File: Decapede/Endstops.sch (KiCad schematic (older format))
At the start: 30 parts, among them P22 X_min, P23 X_max, P24 Y_min, P25 Y_max, P26 Z_min, P27 Z_max, P28 W_min, P29 W_max, P30 V_min, P31 V_max, P32 A_min, P33 A_max, P34 B_min, P35 B_max, P36 C_min, P37 C_max, P38 D_min, P39 D_max, P40 E_min, P41 E_max

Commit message: Updates for Decapede project.
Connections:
- net +5V renamed +V_LOGIC
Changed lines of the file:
@@
 Sheet 5 10
 Title "Endstop connectors"
-Date "19 jan 2014"
+Date "26 jan 2014"
 Rev ""
 Comp ""
@@
 	1    0    0    -1
 $EndComp
-$Comp
-L +5V #PWR0106
-U 1 1 52DC35DB
-P 1600 1000
-F 0 "#PWR0106" H 1600 1090 20  0001 C CNN
-F 1 "+5V" H 1600 1090 30  0000 C CNN
-F 2 "" H 1600 1000 60  0000 C CNN
-F 3 "" H 1600 1000 60  0000 C CNN
-	1    1600 1000
-	1    0    0    -1
-$EndComp
 Wire Wire Line
 	2050 1250 1450 1250
@@
 	1700 1750 1700 1250
 Connection ~ 1700 1250
-$Comp
-L GND #PWR0107
-U 1 1 52DC3617
-P 1900 2050
-F 0 "#PWR0107" H 1900 2050 30  0001 C CNN
-F 1 "GND" H 1900 1980 30  0001 C CNN
-F 2 "" H 1900 2050 60  0000 C CNN
-F 3 "" H 1900 2050 60  0000 C CNN
-	1    1900 2050
-	1    0    0    -1
-$EndComp
 Wire Wire Line
 	1900 2050 1900 1850
@@
 	1700 3050 1700 2550
 Connection ~ 1700 2550
-$Comp
-L GND #PWR0108
-U 1 1 52DC3687
-P 1900 3350
-F 0 "#PWR0108" H 1900 3350 30  0001 C CNN
-F 1 "GND" H 1900 3280 30  0001 C CNN
-F 2 "" H 1900 3350 60  0000 C CNN
-F 3 "" H 1900 3350 60  0000 C CNN
-	1    1900 3350
-	1    0    0    -1
-$EndComp
 Wire Wire Line
 	1900 3350 1900 3150
@@
 	1700 4300 1700 3800
 Connection ~ 1700 3800
-$Comp
-L GND #PWR0109
-U 1 1 52DC36C9
-P 1900 4600
-F 0 "#PWR0109" H 1900 4600 30  0001 C CNN
-F 1 "GND" H 1900 4530 30  0001 C CNN
-F 2 "" H 1900 4600 60  0000 C CNN
-F 3 "" H 1900 4600 60  0000 C CNN
-	1    1900 4600
-	1    0    0    -1
-$EndComp
 Wire Wire Line
 	1900 4600 1900 4400
@@
 	1700 5600 1700 5100
 Connection ~ 1700 5100
-$Comp
-L GND #PWR0110
-U 1 1 52DC36F3
-P 1900 5900
-F 0 "#PWR0110" H 1900 5900 30  0001 C CNN
-F 1 "GND" H 1900 5830 30  0001 C CNN
-F 2 "" H 1900 5900 60  0000 C CNN
-F 3 "" H 1900 5900 60  0000 C CNN
-	1    1900 5900
-	1    0    0    -1
-$EndComp
 Wire Wire Line
 	1900 5900 1900 5700
@@
 	1700 7000 1700 6500
 Connection ~ 1700 6500
-$Comp
-L GND #PWR0111
-U 1 1 52DC371D
-P 1900 7300
-F 0 "#PWR0111" H 1900 7300 30  0001 C CNN
-F 1 "GND" H 1900 7230 30  0001 C CNN
-F 2 "" H 1900 7300 60  0000 C CNN
-F 3 "" H 1900 7300 60  0000 C CNN
-	1    1900 7300
-	1    0    0    -1
-$EndComp
 Wire Wire Line
 	1900 7300 1900 7100
@@
 	4850 1750 4850 1250
 Connection ~ 4850 1250
-$Comp
-L GND #PWR0112
-U 1 1 52DC3747
-P 5050 2050
-F 0 "#PWR0112" H 5050 2050 30  0001 C CNN
-F 1 "GND" H 5050 1980 30  0001 C CNN
-F 2 "" H 5050 2050 60  0000 C CNN
-F 3 "" H 5050 2050 60  0000 C CNN
-	1    5050 2050
-	1    0    0    -1
-$EndComp
 Wire Wire Line
 	5050 2050 5050 1850
@@
 	4850 3050 4850 2550
 Connection ~ 4850 2550
-$Comp
-L GND #PWR0113
-U 1 1 52DC3771
-P 5050 3350
-F 0 "#PWR0113" H 5050 3350 30  0001 C CNN
-F 1 "GND" H 5050 3280 30  0001 C CNN
-F 2 "" H 5050 3350 60  0000 C CNN
-F 3 "" H 5050 3350 60  0000 C CNN
-	1    5050 3350
-	1    0    0    -1
-$EndComp
 Wire Wire Line
 	5050 3350 5050 3150
@@
 	4850 4300 4850 3800
 Connection ~ 4850 3800
-$Comp
-L GND #PWR0114
-U 1 1 52DC379B
-P 5050 4600
-F 0 "#PWR0114" H 5050 4600 30  0001 C CNN
-F 1 "GND" H 5050 4530 30  0001 C CNN
-F 2 "" H 5050 4600 60  0000 C CNN
-F 3 "" H 5050 4600 60  0000 C CNN
-	1    5050 4600
-	1    0    0    -1
-$EndComp
 Wire Wire Line
 	5050 4600 5050 4400
@@
 	4850 5600 4850 5100
 Connection ~ 4850 5100
-$Comp
-L GND #PWR0115
-U 1 1 52DC37C5
-P 5050 5900
-F 0 "#PWR0115" H 5050 5900 30  0001 C CNN
-F 1 "GND" H 5050 5830 30  0001 C CNN
-F 2 "" H 5050 5900 60  0000 C CNN
-F 3 "" H 5050 5900 60  0000 C CNN
-	1    5050 5900
-	1    0    0    -1
-$EndComp
 Wire Wire Line
 	5050 5900 5050 5700
@@
 	4850 7000 4850 6500
 Connection ~ 4850 6500
-$Comp
-L GND #PWR0116
-U 1 1 52DC37EF
-P 5050 7300
-F 0 "#PWR0116" H 5050 7300 30  0001 C CNN
-F 1 "GND" H 5050 7230 30  0001 C CNN
-F 2 "" H 5050 7300 60  0000 C CNN
-F 3 "" H 5050 7300 60  0000 C CNN
-	1    5050 7300
-	1    0    0    -1
-$EndComp
 Wire Wire Line
 	5050 7300 5050 7100
@@
 Connection ~ 1600 4500
 Connection ~ 1600 5800
-$Comp
-L +5V #PWR0117
-U 1 1 52DC3C0A
-P 4750 1000
-F 0 "#PWR0117" H 4750 1090 20  0001 C CNN
-F 1 "+5V" H 4750 1090 30  0000 C CNN
-F 2 "" H 4750 1000 60  0000 C CNN
-F 3 "" H 4750 1000 60  0000 C CNN
-	1    4750 1000
-	1    0    0    -1
-$EndComp
 Wire Wire Line
 	4750 1000 4750 7200
@@
 Connection ~ 4750 4500
 Connection ~ 4750 5800
+$Comp
+L +V_LOGIC #PWR0119
+U 1 1 52E043B0
+P 1600 1000
+F 0 "#PWR0119" H 1600 970 30  0001 C CNN
+F 1 "+V_LOGIC" H 1600 1100 30  0000 C CNN
+F 2 "~" H 1600 1000 60  0000 C CNN
+F 3 "~" H 1600 1000 60  0000 C CNN
+	1    1600 1000
+	1    0    0    -1
+$EndComp
+$Comp
+L +V_LOGIC #PWR0120
+U 1 1 52E043BF
+P 4750 1000
+F 0 "#PWR0120" H 4750 970 30  0001 C CNN
+F 1 "+V_LOGIC" H 4750 1100 30  0000 C CNN
+F 2 "~" H 4750 1000 60  0000 C CNN
+F 3 "~" H 4750 1000 60  0000 C CNN
+	1    4750 1000
+	1    0    0    -1
+$EndComp
+$Comp
+L GND #PWR0121
+U 1 1 52E17455
+P 1900 2050
+F 0 "#PWR0121" H 1900 2050 30  0001 C CNN
+F 1 "GND" H 1900 1980 30  0001 C CNN
+F 2 "" H 1900 2050 60  0000 C CNN
+F 3 "" H 1900 2050 60  0000 C CNN
+	1    1900 2050
+	1    0    0    -1
+$EndComp
+$Comp
+L GND #PWR0122
+U 1 1 52E17462
+P 1900 3350
+F 0 "#PWR0122" H 1900 3350 30  0001 C CNN
+F 1 "GND" H 1900 3280 30  0001 C CNN
+F 2 "" H 1900 3350 60  0000 C CNN
+F 3 "" H 1900 3350 60  0000 C CNN
+	1    1900 3350
+	1    0    0    -1
+$EndComp
+$Comp
+L GND #PWR0123
+U 1 1 52E17468
+P 5050 2050
+F 0 "#PWR0123" H 5050 2050 30  0001 C CNN
+F 1 "GND" H 5050 1980 30  0001 C CNN
+F 2 "" H 5050 2050 60  0000 C CNN
+F 3 "" H 5050 2050 60  0000 C CNN
+	1    5050 2050
+	1    0    0    -1
+$EndComp
+$Comp
+L GND #PWR0124
+U 1 1 52E1746E
+P 5050 3350
+F 0 "#PWR0124" H 5050 3350 30  0001 C CNN
+F 1 "GND" H 5050 3280 30  0001 C CNN
+F 2 "" H 5050 3350 60  0000 C CNN
+F 3 "" H 5050 3350 60  0000 C CNN
+	1    5050 3350
+	1    0    0    -1
+$EndComp
+$Comp
+L GND #PWR0125
+U 1 1 52E17474
+P 1900 4600
+F 0 "#PWR0125" H 1900 4600 30  0001 C CNN
+F 1 "GND" H 1900 4530 30  0001 C CNN
+F 2 "" H 1900 4600 60  0000 C CNN
+F 3 "" H 1900 4600 60  0000 C CNN
+	1    1900 4600
+	1    0    0    -1
+$EndComp
+$Comp
+L GND #PWR0126
+U 1 1 52E1747A
+P 5050 4600
+F 0 "#PWR0126" H 5050 4600 30  0001 C CNN
+F 1 "GND" H 5050 4530 30  0001 C CNN
+F 2 "" H 5050 4600 60  0000 C CNN
+F 3 "" H 5050 4600 60  0000 C CNN
+	1    5050 4600
+	1    0    0    -1
+$EndComp
+$Comp
+L GND #PWR0127
+U 1 1 52E17480
+P 5050 5900
+F 0 "#PWR0127" H 5050 5900 30  0001 C CNN
+F 1 "GND" H 5050 5830 30  0001 C CNN
+F 2 "" H 5050 5900 60  0000 C CNN
+F 3 "" H 5050 5900 60  0000 C CNN
+	1    5050 5900
+	1    0    0    -1
+$EndComp
+$Comp
+L GND #PWR0128
+U 1 1 52E17486
+P 1900 5900
+F 0 "#PWR0128" H 1900 5900 30  0001 C CNN
+F 1 "GND" H 1900 5830 30  0001 C CNN
+F 2 "" H 1900 5900 60  0000 C CNN
+F 3 "" H 1900 5900 60  0000 C CNN
+	1    1900 5900
+	1    0    0    -1
+$EndComp
+$Comp
+L GND #PWR0129
+U 1 1 52E1748C
+P 1900 7300
+F 0 "#PWR0129" H 1900 7300 30  0001 C CNN
+F 1 "GND" H 1900 7230 30  0001 C CNN
+F 2 "" H 1900 7300 60  0000 C CNN
+F 3 "" H 1900 7300 60  0000 C CNN
+	1    1900 7300
+	1    0    0    -1
+$EndComp
+$Comp
+L GND #PWR0130
+U 1 1 52E17492
+P 5050 7300
+F 0 "#PWR0130" H 5050 7300 30  0001 C CNN
+F 1 "GND" H 5050 7230 30  0001 C CNN
+F 2 "" H 5050 7300 60  0000 C CNN
+F 3 "" H 5050 7300 60  0000 C CNN
+	1    5050 7300
+	1    0    0    -1
+$EndComp
 $EndSCHEMATC

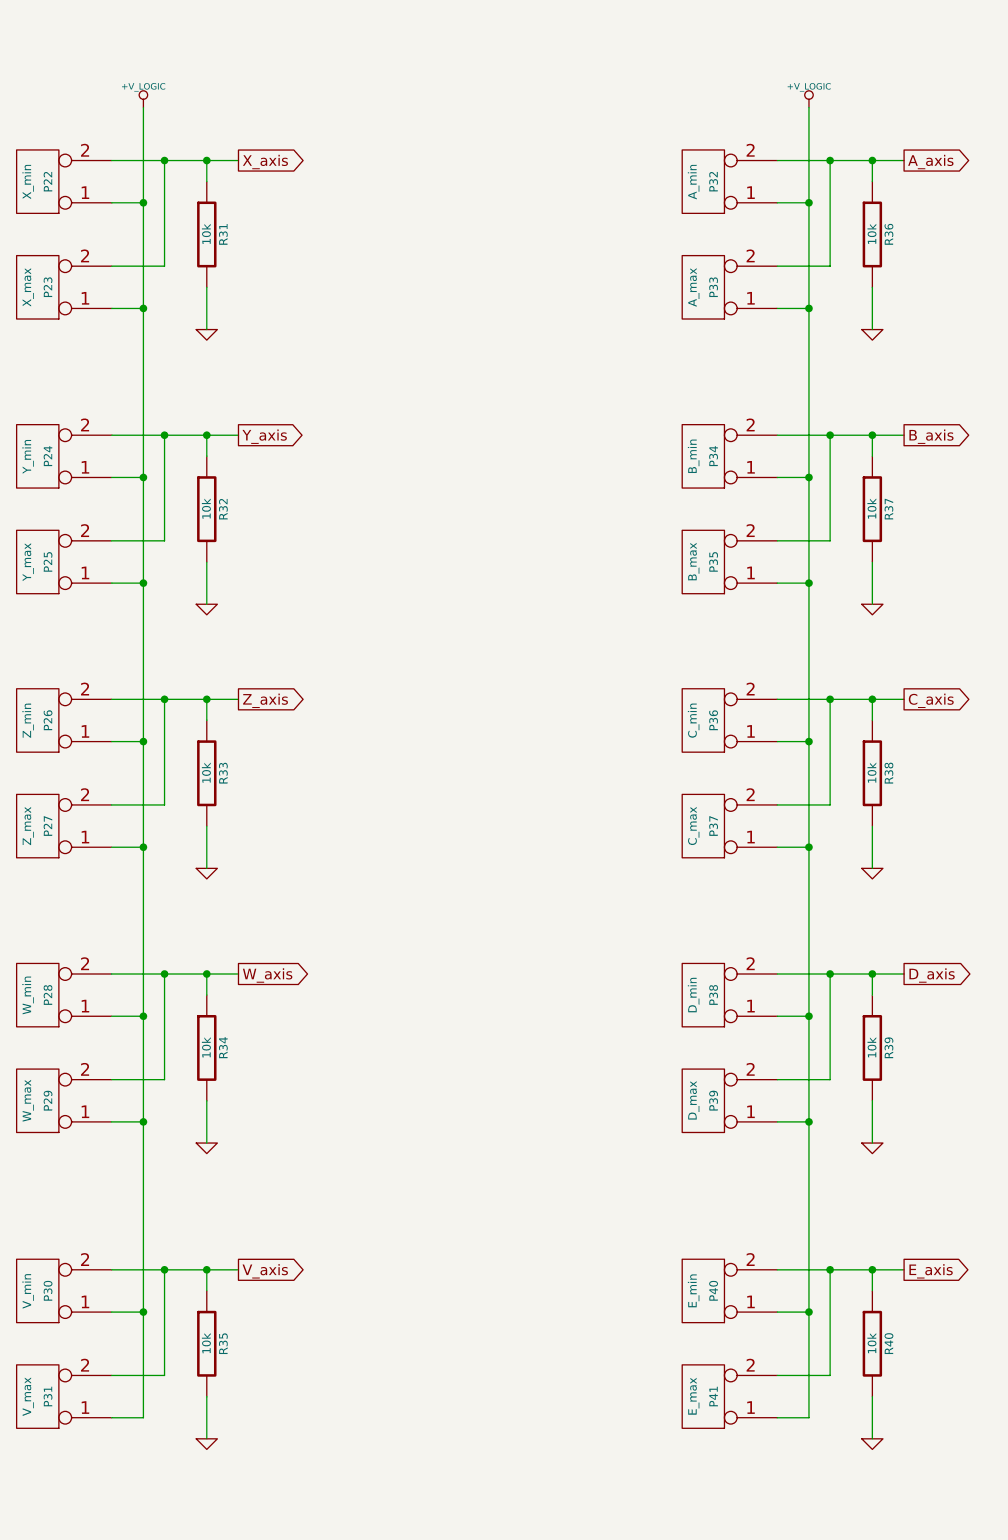
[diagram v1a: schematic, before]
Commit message: Decapede update: add fuses for each main section; change endstops to use 0V instead of 5V; more space for stepper drivers to allow latching connectors
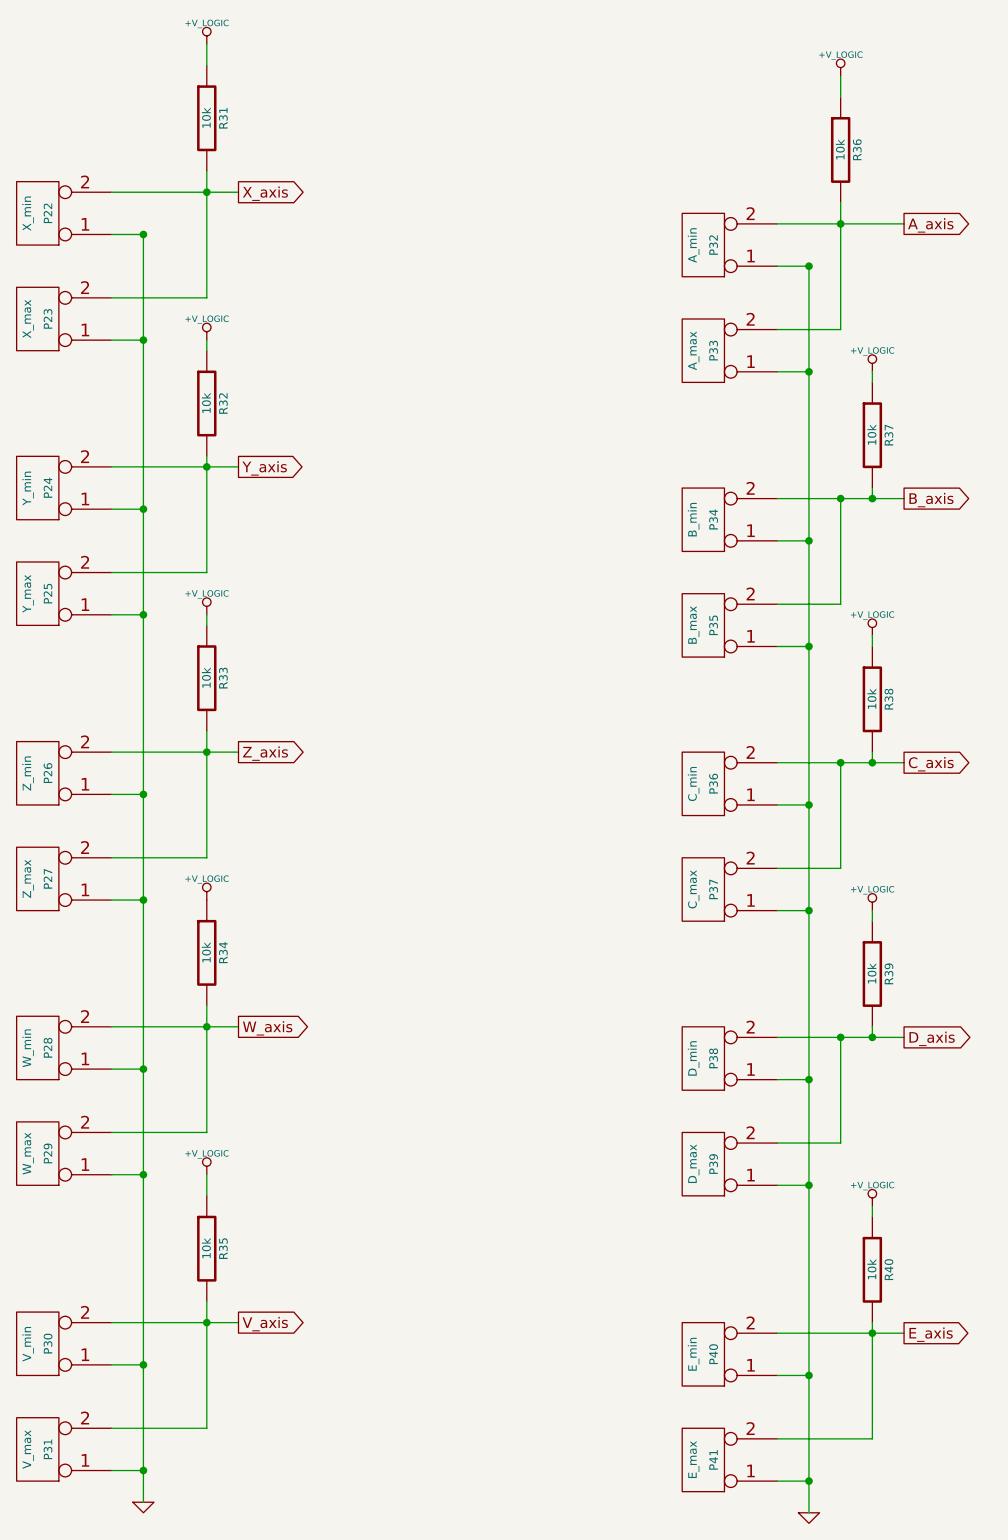
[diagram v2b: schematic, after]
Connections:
- net +V_LOGIC: now also R31.1, R32.1, R33.1, R34.1, R35.1, R36.1, R37.1, R38.1, R39.1, R40.1; no longer P22.1 (P1), P23.1 (P1), P24.1 (P1), P25.1 (P1), P26.1 (P1), P27.1 (P1), P28.1 (P1), P29.1 (P1), P30.1 (P1), P31.1 (P1), P32.1 (P1), P33.1 (P1), P34.1 (P1), P35.1 (P1), P36.1 (P1), P37.1 (P1), P38.1 (P1), P39.1 (P1), P40.1 (P1), P41.1 (P1)
- net A_axis: now also R36.2; no longer R36.1
- net B_axis: now also R37.2; no longer R37.1
- net C_axis: now also R38.2; no longer R38.1
- net D_axis: now also R39.2; no longer R39.1
- net E_axis: now also R40.2; no longer R40.1
- net GND: now also P22.1 (P1), P23.1 (P1), P24.1 (P1), P25.1 (P1), P26.1 (P1), P27.1 (P1), P28.1 (P1), P29.1 (P1), P30.1 (P1), P31.1 (P1), P32.1 (P1), P33.1 (P1), P34.1 (P1), P35.1 (P1), P36.1 (P1), P37.1 (P1), P38.1 (P1), P39.1 (P1), P40.1 (P1), P41.1 (P1); no longer R31.2, R32.2, R33.2, R34.2, R35.2, R36.2, R37.2, R38.2, R39.2, R40.2
- net V_axis: now also R35.2; no longer R35.1
- net W_axis: now also R34.2; no longer R34.1
- net X_axis: now also R31.2; no longer R31.1
- net Y_axis: now also R32.2; no longer R32.1
- net Z_axis: now also R33.2; no longer R33.1
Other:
- moved on the sheet: P22, P23, P24, P25, P26, P27, P28, P29, P30, P31, P32, P33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
